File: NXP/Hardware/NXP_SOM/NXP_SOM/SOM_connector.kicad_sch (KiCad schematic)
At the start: 1 part, among them J2 10164228-1001A1RLF

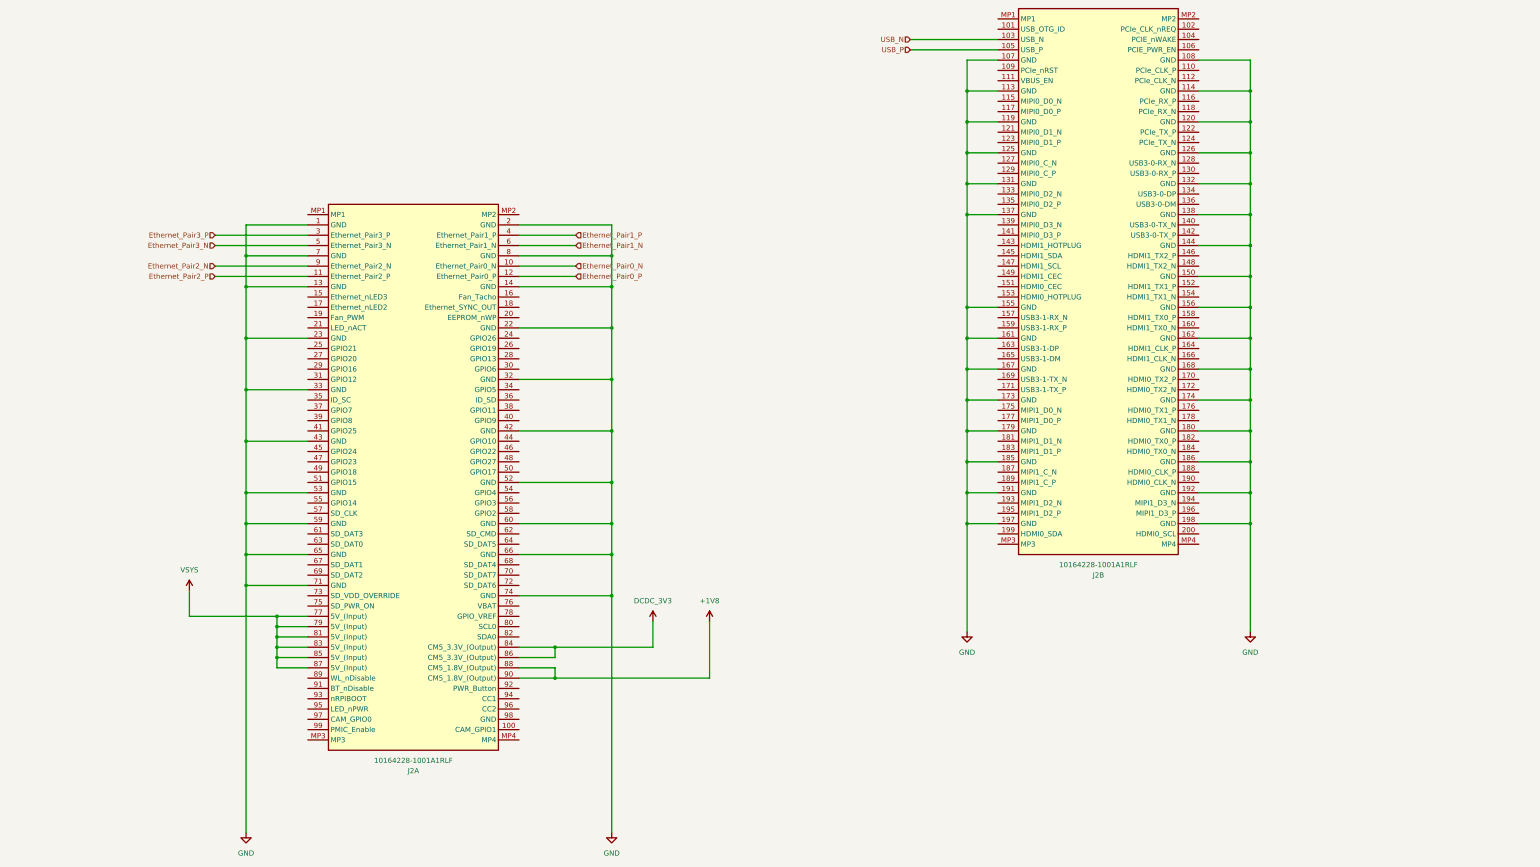
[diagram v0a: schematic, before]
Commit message: connected RAM to SOM
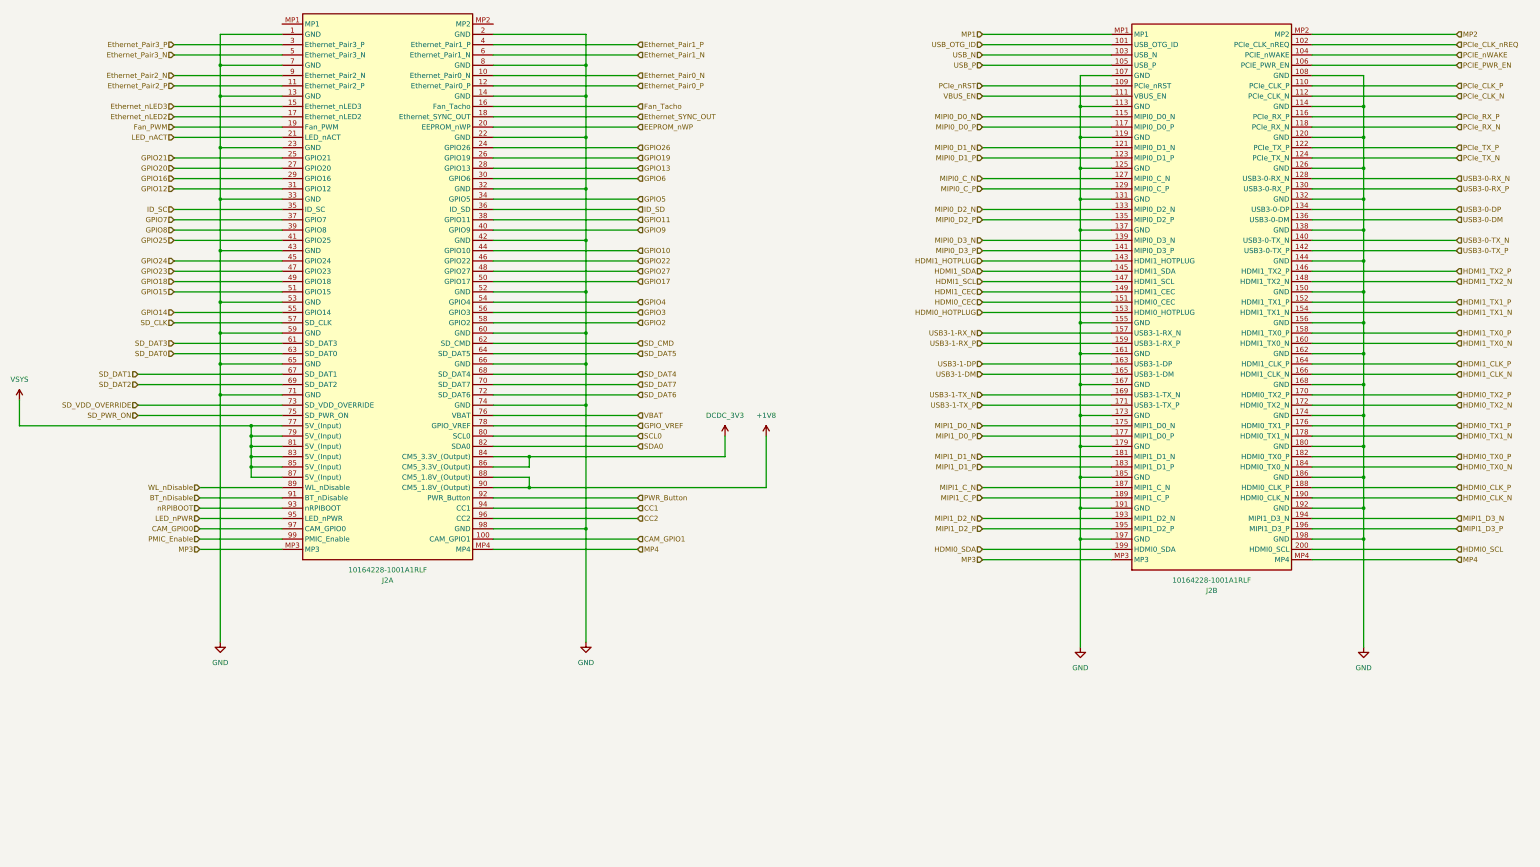
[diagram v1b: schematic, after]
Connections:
- net GND: now also J2.98 (GND)
- net CAM_GPIO1: now reaches J2.100 (CAM_GPIO1)
- net Ethernet_nLED3: now reaches J2.15 (Ethernet_nLED3)
- net Fan_Tacho: now reaches J2.16 (Fan_Tacho)
- net Ethernet_nLED2: now reaches J2.17 (Ethernet_nLED2)
- net Ethernet_SYNC_OUT: now reaches J2.18 (Ethernet_SYNC_OUT)
- net Fan_PWM: now reaches J2.19 (Fan_PWM)
- net EEPROM_nWP: now reaches J2.20 (EEPROM_nWP)
- net LED_nACT: now reaches J2.21 (LED_nACT)
- net GPIO26: now reaches J2.24 (GPIO26)
- net GPIO21: now reaches J2.25 (GPIO21)
- net GPIO19: now reaches J2.26 (GPIO19)
- net GPIO20: now reaches J2.27 (GPIO20)
- net GPIO13: now reaches J2.28 (GPIO13)
- net GPIO16: now reaches J2.29 (GPIO16)
- net GPIO6: now reaches J2.30 (GPIO6)
- net GPIO12: now reaches J2.31 (GPIO12)
- net GPIO5: now reaches J2.34 (GPIO5)
- net ID_SC: now reaches J2.35 (ID_SC)
- net ID_SD: now reaches J2.36 (ID_SD)
- net GPIO7: now reaches J2.37 (GPIO7)
- net GPIO11: now reaches J2.38 (GPIO11)
- net GPIO8: now reaches J2.39 (GPIO8)
- net GPIO9: now reaches J2.40 (GPIO9)
- net GPIO25: now reaches J2.41 (GPIO25)
- net GPIO10: now reaches J2.44 (GPIO10)
- net GPIO24: now reaches J2.45 (GPIO24)
- net GPIO22: now reaches J2.46 (GPIO22)
- net GPIO23: now reaches J2.47 (GPIO23)
- net GPIO27: now reaches J2.48 (GPIO27)
- net GPIO18: now reaches J2.49 (GPIO18)
- net GPIO17: now reaches J2.50 (GPIO17)
- net GPIO15: now reaches J2.51 (GPIO15)
- net GPIO4: now reaches J2.54 (GPIO4)
- net GPIO14: now reaches J2.55 (GPIO14)
- net GPIO3: now reaches J2.56 (GPIO3)
- net SD_CLK: now reaches J2.57 (SD_CLK)
- net GPIO2: now reaches J2.58 (GPIO2)
- net SD_DAT3: now reaches J2.61 (SD_DAT3)
- net SD_CMD: now reaches J2.62 (SD_CMD)
- net SD_DAT0: now reaches J2.63 (SD_DAT0)
- net SD_DAT5: now reaches J2.64 (SD_DAT5)
- net SD_DAT1: now reaches J2.67 (SD_DAT1)
- net SD_DAT4: now reaches J2.68 (SD_DAT4)
- net SD_DAT2: now reaches J2.69 (SD_DAT2)
- net SD_DAT7: now reaches J2.70 (SD_DAT7)
- net SD_DAT6: now reaches J2.72 (SD_DAT6)
- net SD_VDD_OVERRIDE: now reaches J2.73 (SD_VDD_OVERRIDE)
- net SD_PWR_ON: now reaches J2.75 (SD_PWR_ON)
- net VBAT: now reaches J2.76 (VBAT)
- net GPIO_VREF: now reaches J2.78 (GPIO_VREF)
- net SCL0: now reaches J2.80 (SCL0)
- net SDA0: now reaches J2.82 (SDA0)
- net WL_nDisable: now reaches J2.89 (WL_nDisable)
- net BT_nDisable: now reaches J2.91 (BT_nDisable)
- net PWR_Button: now reaches J2.92 (PWR_Button)
- net nRPIBOOT: now reaches J2.93 (nRPIBOOT)
- net CC1: now reaches J2.94 (CC1)
- net LED_nPWR: now reaches J2.95 (LED_nPWR)
- net CC2: now reaches J2.96 (CC2)
- net CAM_GPIO0: now reaches J2.97 (CAM_GPIO0)
- net PMIC_Enable: now reaches J2.99 (PMIC_Enable)
- net MP3: now reaches J2.MP3
- net MP3: now also J2.MP3
- net MP4: now reaches J2.MP4
- net MP4: now also J2.MP4
- net USB_OTG_ID: now reaches J2.101 (USB_OTG_ID)
- net PCIe_CLK_nREQ: now reaches J2.102 (PCIe_CLK_nREQ)
- net PCIE_nWAKE: now reaches J2.104 (PCIE_nWAKE)
- net PCIE_PWR_EN: now reaches J2.106 (PCIE_PWR_EN)
- net PCIe_nRST: now reaches J2.109 (PCIe_nRST)
- net PCIe_CLK_P: now reaches J2.110 (PCIe_CLK_P)
- net VBUS_EN: now reaches J2.111 (VBUS_EN)
- net PCIe_CLK_N: now reaches J2.112 (PCIe_CLK_N)
- net MIPI0_D0_N: now reaches J2.115 (MIPI0_D0_N)
- net PCIe_RX_P: now reaches J2.116 (PCIe_RX_P)
- net MIPI0_D0_P: now reaches J2.117 (MIPI0_D0_P)
- net PCIe_RX_N: now reaches J2.118 (PCIe_RX_N)
- net MIPI0_D1_N: now reaches J2.121 (MIPI0_D1_N)
- net PCIe_TX_P: now reaches J2.122 (PCIe_TX_P)
- net MIPI0_D1_P: now reaches J2.123 (MIPI0_D1_P)
- net PCIe_TX_N: now reaches J2.124 (PCIe_TX_N)
- net MIPI0_C_N: now reaches J2.127 (MIPI0_C_N)
- net USB3-0-RX_N: now reaches J2.128 (USB3-0-RX_N)
- net MIPI0_C_P: now reaches J2.129 (MIPI0_C_P)
- net USB3-0-RX_P: now reaches J2.130 (USB3-0-RX_P)
- net MIPI0_D2_N: now reaches J2.133 (MIPI0_D2_N)
- net USB3-0-DP: now reaches J2.134 (USB3-0-DP)
- net MIPI0_D2_P: now reaches J2.135 (MIPI0_D2_P)
- net USB3-0-DM: now reaches J2.136 (USB3-0-DM)
- net MIPI0_D3_N: now reaches J2.139 (MIPI0_D3_N)
- net USB3-0-TX_N: now reaches J2.140 (USB3-0-TX_N)
- net MIPI0_D3_P: now reaches J2.141 (MIPI0_D3_P)
- net USB3-0-TX_P: now reaches J2.142 (USB3-0-TX_P)
- net HDMI1_HOTPLUG: now reaches J2.143 (HDMI1_HOTPLUG)
- net HDMI1_SDA: now reaches J2.145 (HDMI1_SDA)
- net HDMI1_TX2_P: now reaches J2.146 (HDMI1_TX2_P)
- net HDMI1_SCL: now reaches J2.147 (HDMI1_SCL)
- net HDMI1_TX2_N: now reaches J2.148 (HDMI1_TX2_N)
- net HDMI1_CEC: now reaches J2.149 (HDMI1_CEC)
- net HDMI0_CEC: now reaches J2.151 (HDMI0_CEC)
- net HDMI1_TX1_P: now reaches J2.152 (HDMI1_TX1_P)
- net HDMI0_HOTPLUG: now reaches J2.153 (HDMI0_HOTPLUG)
- net HDMI1_TX1_N: now reaches J2.154 (HDMI1_TX1_N)
- net USB3-1-RX_N: now reaches J2.157 (USB3-1-RX_N)
- net HDMI1_TX0_P: now reaches J2.158 (HDMI1_TX0_P)
- net USB3-1-RX_P: now reaches J2.159 (USB3-1-RX_P)
- net HDMI1_TX0_N: now reaches J2.160 (HDMI1_TX0_N)
- net USB3-1-DP: now reaches J2.163 (USB3-1-DP)
- net HDMI1_CLK_P: now reaches J2.164 (HDMI1_CLK_P)
- net USB3-1-DM: now reaches J2.165 (USB3-1-DM)
- net HDMI1_CLK_N: now reaches J2.166 (HDMI1_CLK_N)
- net USB3-1-TX_N: now reaches J2.169 (USB3-1-TX_N)
- net HDMI0_TX2_P: now reaches J2.170 (HDMI0_TX2_P)
- net USB3-1-TX_P: now reaches J2.171 (USB3-1-TX_P)
- net HDMI0_TX2_N: now reaches J2.172 (HDMI0_TX2_N)
- net MIPI1_D0_N: now reaches J2.175 (MIPI1_D0_N)
- net HDMI0_TX1_P: now reaches J2.176 (HDMI0_TX1_P)
- net MIPI1_D0_P: now reaches J2.177 (MIPI1_D0_P)
- net HDMI0_TX1_N: now reaches J2.178 (HDMI0_TX1_N)
- net MIPI1_D1_N: now reaches J2.181 (MIPI1_D1_N)
- net HDMI0_TX0_P: now reaches J2.182 (HDMI0_TX0_P)
- net MIPI1_D1_P: now reaches J2.183 (MIPI1_D1_P)
- net HDMI0_TX0_N: now reaches J2.184 (HDMI0_TX0_N)
- net MIPI1_C_N: now reaches J2.187 (MIPI1_C_N)
- net HDMI0_CLK_P: now reaches J2.188 (HDMI0_CLK_P)
- net MIPI1_C_P: now reaches J2.189 (MIPI1_C_P)
- net HDMI0_CLK_N: now reaches J2.190 (HDMI0_CLK_N)
- net MIPI1_D2_N: now reaches J2.193 (MIPI1_D2_N)
- net MIPI1_D3_N: now reaches J2.194 (MIPI1_D3_N)
- net MIPI1_D2_P: now reaches J2.195 (MIPI1_D2_P)
- net MIPI1_D3_P: now reaches J2.196 (MIPI1_D3_P)
- net HDMI0_SDA: now reaches J2.199 (HDMI0_SDA)
- net HDMI0_SCL: now reaches J2.200 (HDMI0_SCL)
- net MP1: now reaches J2.MP1
- net MP2: now reaches J2.MP2
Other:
- moved on the sheet: J2A, J2B
